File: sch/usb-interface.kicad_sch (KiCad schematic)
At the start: 4 parts, among them IC1 USB2244I-AEZG-06

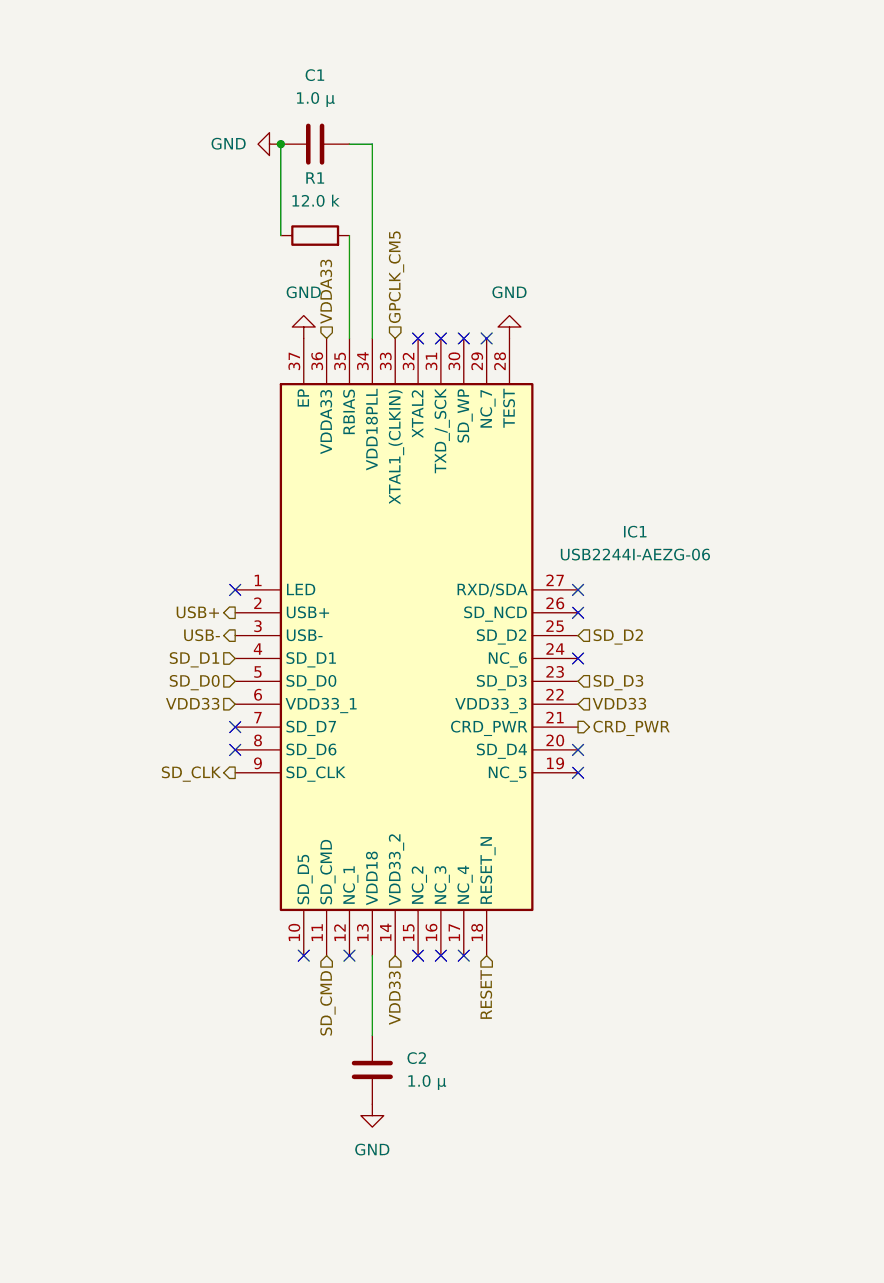
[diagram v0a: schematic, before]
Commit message: Added ports to CM5 and USB interface and connected them
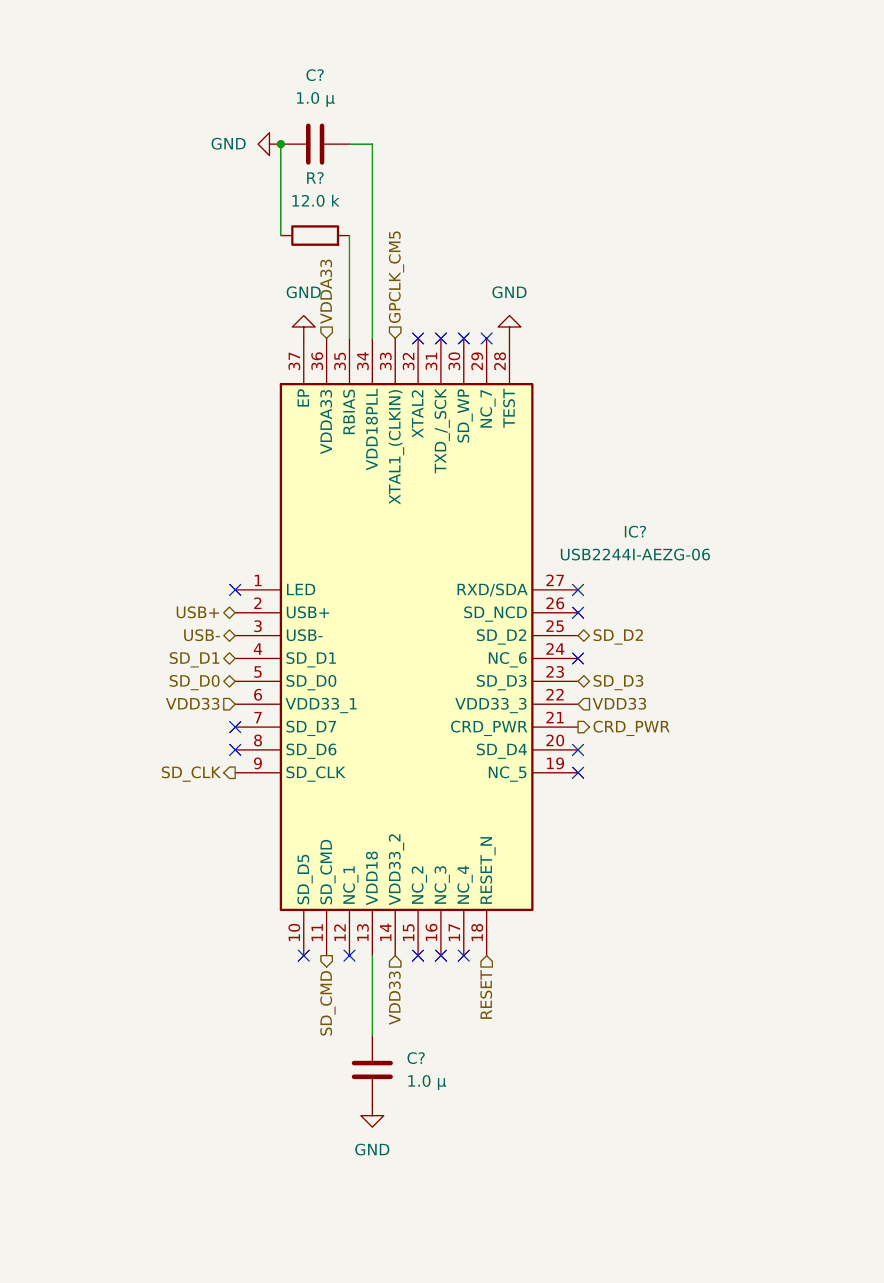
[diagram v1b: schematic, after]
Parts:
- renumbered C1 to C?, C2 to C?, IC1 to IC?, R1 to R?
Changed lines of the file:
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@@
 	)
 	(hierarchical_label "SD_D1"
-		(shape input)
+		(shape bidirectional)
 		(at 68.58 92.71 180)
 		(effects
@@
 	)
 	(hierarchical_label "SD_CMD"
-		(shape input)
+		(shape output)
 		(at 78.74 125.73 270)
 		(effects
@@
 	)
 	(hierarchical_label "SD_D3"
-		(shape input)
+		(shape bidirectional)
 		(at 106.68 95.25 0)
 		(effects
@@
 	)
 	(hierarchical_label "USB-"
-		(shape output)
+		(shape bidirectional)
 		(at 68.58 90.17 180)
 		(effects
@@
 	)
 	(hierarchical_label "SD_D0"
-		(shape input)
+		(shape bidirectional)
 		(at 68.58 95.25 180)
 		(effects
@@
 	)
 	(hierarchical_label "SD_D2"
-		(shape input)
+		(shape bidirectional)
 		(at 106.68 90.17 0)
 		(effects
@@
 	)
 	(hierarchical_label "USB+"
-		(shape output)
+		(shape bidirectional)
 		(at 68.58 87.63 180)
 		(effects
@@
 		(dnp no)
 		(fields_autoplaced yes)
-		(property "Reference" "#PWR04"
+		(property "Reference" "#PWR?"
 			(at 83.82 148.59 0)
 			(effects
@@
 		)
 		(instances
+			(project "audiograb"
+				(path "/c46c2311-6d4b-411d-b012-c7730eac136d/53f9c81a-1433-4854-9dfc-932cf29aee40"
+					(reference "#PWR?")
+					(unit 1)
+				)
+			)
 			(project "usb-interface"
 				(path "/eaea460a-c66f-4f33-a920-83ec112e8ee3"
@@
 		(dnp no)
 		(fields_autoplaced yes)
-		(property "Reference" "C1"
+		(property "Reference" "C?"
 			(at 77.47 27.94 90)
 			(effects
@@
 		)
 		(instances
+			(project "audiograb"
+				(path "/c46c2311-6d4b-411d-b012-c7730eac136d/53f9c81a-1433-4854-9dfc-932cf29aee40"
+					(reference "C?")
+					(unit 1)
+				)
+			)
 			(project ""
 				(path "/eaea460a-c66f-4f33-a920-83ec112e8ee3"
@@
 		(dnp no)
 		(fields_autoplaced yes)
-		(property "Reference" "C2"
+		(property "Reference" "C?"
 			(at 87.63 137.1599 0)
 			(effects
@@
 		)
 		(instances
+			(project "audiograb"
+				(path "/c46c2311-6d4b-411d-b012-c7730eac136d/53f9c81a-1433-4854-9dfc-932cf29aee40"
+					(reference "C?")
+					(unit 1)
+				)
+			)
 			(project ""
 				(path "/eaea460a-c66f-4f33-a920-83ec112e8ee3"
@@
 		(dnp no)
 		(fields_autoplaced yes)
-		(property "Reference" "R1"
+		(property "Reference" "R?"
 			(at 77.47 39.37 90)
 			(effects
@@
 		)
 		(instances
+			(project "audiograb"
+				(path "/c46c2311-6d4b-411d-b012-c7730eac136d/53f9c81a-1433-4854-9dfc-932cf29aee40"
+					(reference "R?")
+					(unit 1)
+				)
+			)
 			(project ""
 				(path "/eaea460a-c66f-4f33-a920-83ec112e8ee3"
@@
 		(dnp no)
 		(fields_autoplaced yes)
-		(property "Reference" "#PWR02"
+		(property "Reference" "#PWR?"
 			(at 99.06 50.8 0)
 			(effects
@@
 		)
 		(instances
+			(project "audiograb"
+				(path "/c46c2311-6d4b-411d-b012-c7730eac136d/53f9c81a-1433-4854-9dfc-932cf29aee40"
+					(reference "#PWR?")
+					(unit 1)
+				)
+			)
 			(project "usb-interface"
 				(path "/eaea460a-c66f-4f33-a920-83ec112e8ee3"
@@
 		(dnp no)
 		(fields_autoplaced yes)
-		(property "Reference" "#PWR01"
+		(property "Reference" "#PWR?"
 			(at 76.2 50.8 0)
 			(effects
@@
 		)
 		(instances
+			(project "audiograb"
+				(path "/c46c2311-6d4b-411d-b012-c7730eac136d/53f9c81a-1433-4854-9dfc-932cf29aee40"
+					(reference "#PWR?")
+					(unit 1)
+				)
+			)
 			(project ""
 				(path "/eaea460a-c66f-4f33-a920-83ec112e8ee3"
@@
 		(dnp no)
 		(fields_autoplaced yes)
-		(property "Reference" "#PWR03"
+		(property "Reference" "#PWR?"
 			(at 67.31 35.56 0)
 			(effects
@@
 		)
 		(instances
+			(project "audiograb"
+				(path "/c46c2311-6d4b-411d-b012-c7730eac136d/53f9c81a-1433-4854-9dfc-932cf29aee40"
+					(reference "#PWR?")
+					(unit 1)
+				)
+			)
 			(project "usb-interface"
 				(path "/eaea460a-c66f-4f33-a920-83ec112e8ee3"
@@
 		(dnp no)
 		(fields_autoplaced yes)
-		(property "Reference" "IC1"
+		(property "Reference" "IC?"
 			(at 113.03 78.6698 0)
 			(effects
@@
 		)
 		(instances
+			(project "audiograb"
+				(path "/c46c2311-6d4b-411d-b012-c7730eac136d/53f9c81a-1433-4854-9dfc-932cf29aee40"
+					(reference "IC?")
+					(unit 1)
+				)
+			)
 			(project ""
 				(path "/eaea460a-c66f-4f33-a920-83ec112e8ee3"

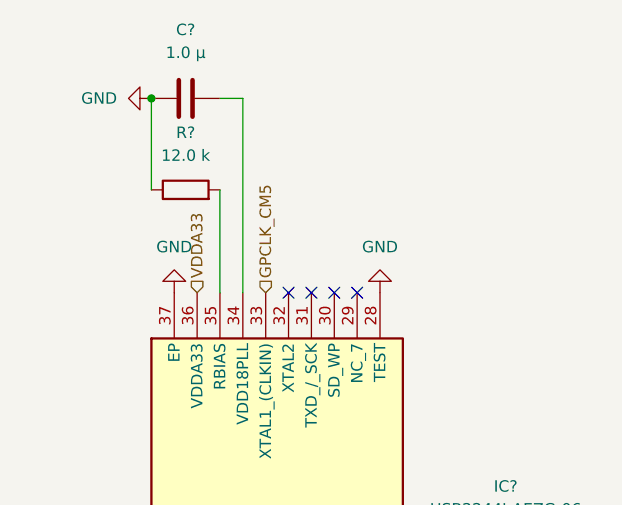
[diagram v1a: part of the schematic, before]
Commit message: Added more ports to the CM5 and connected them
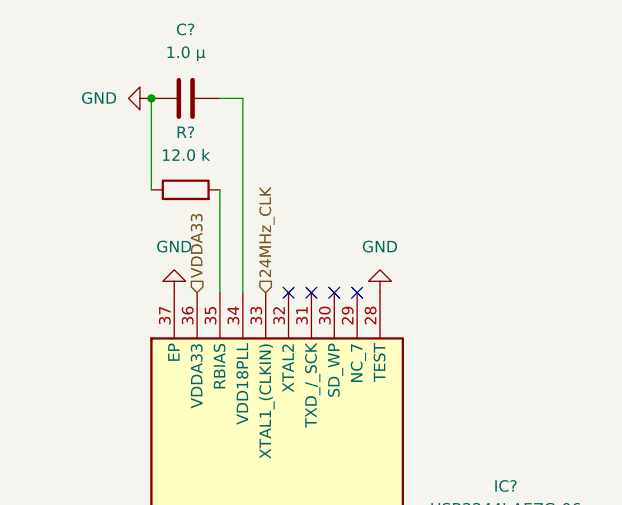
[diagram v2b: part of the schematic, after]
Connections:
- net GPCLK_CM5 renamed 24MHz_CLK
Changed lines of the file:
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@@
 		)
 	)
-	(hierarchical_label "GPCLK_CM5"
+	(hierarchical_label "24MHz_CLK"
 		(shape input)
 		(at 86.36 57.15 90)

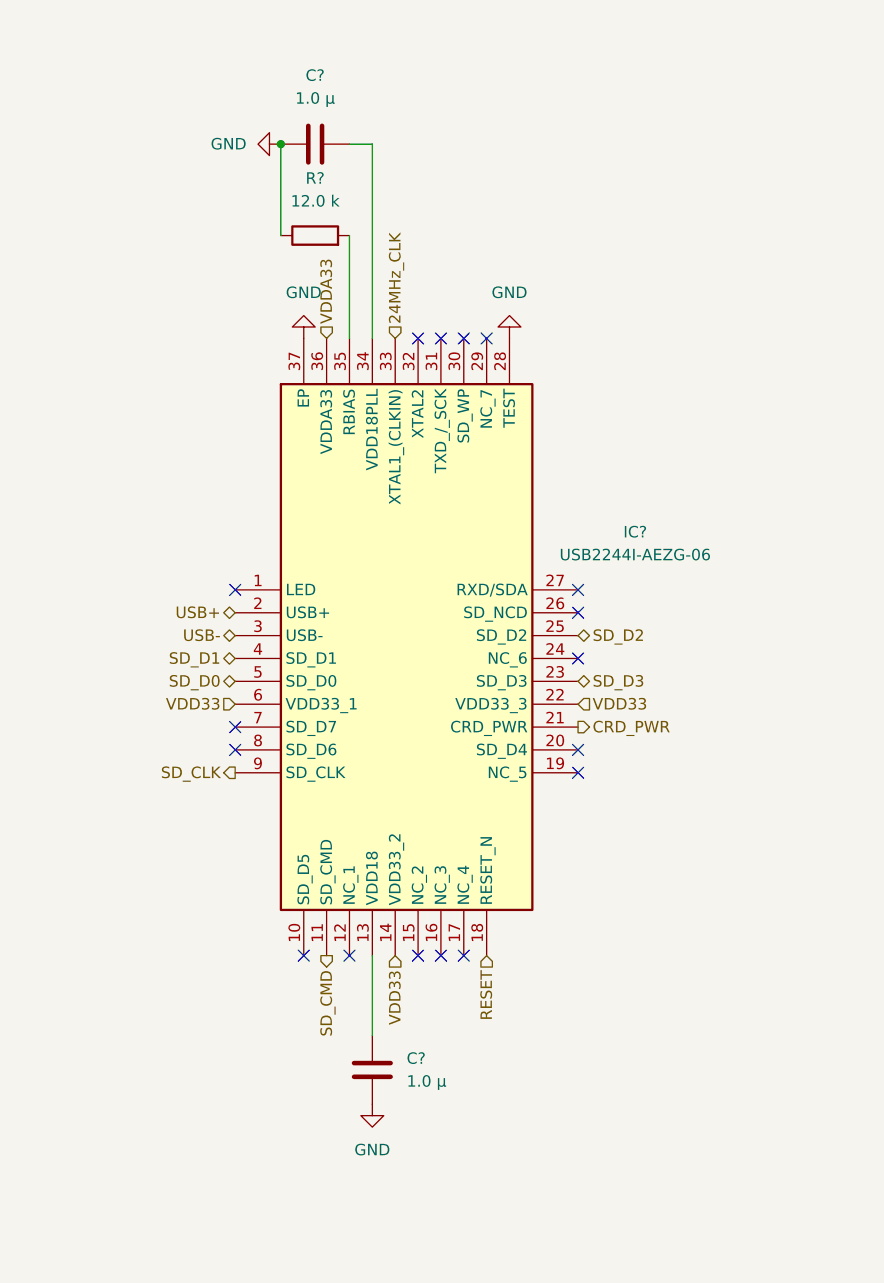
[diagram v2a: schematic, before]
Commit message: added cap footprints and part numbers
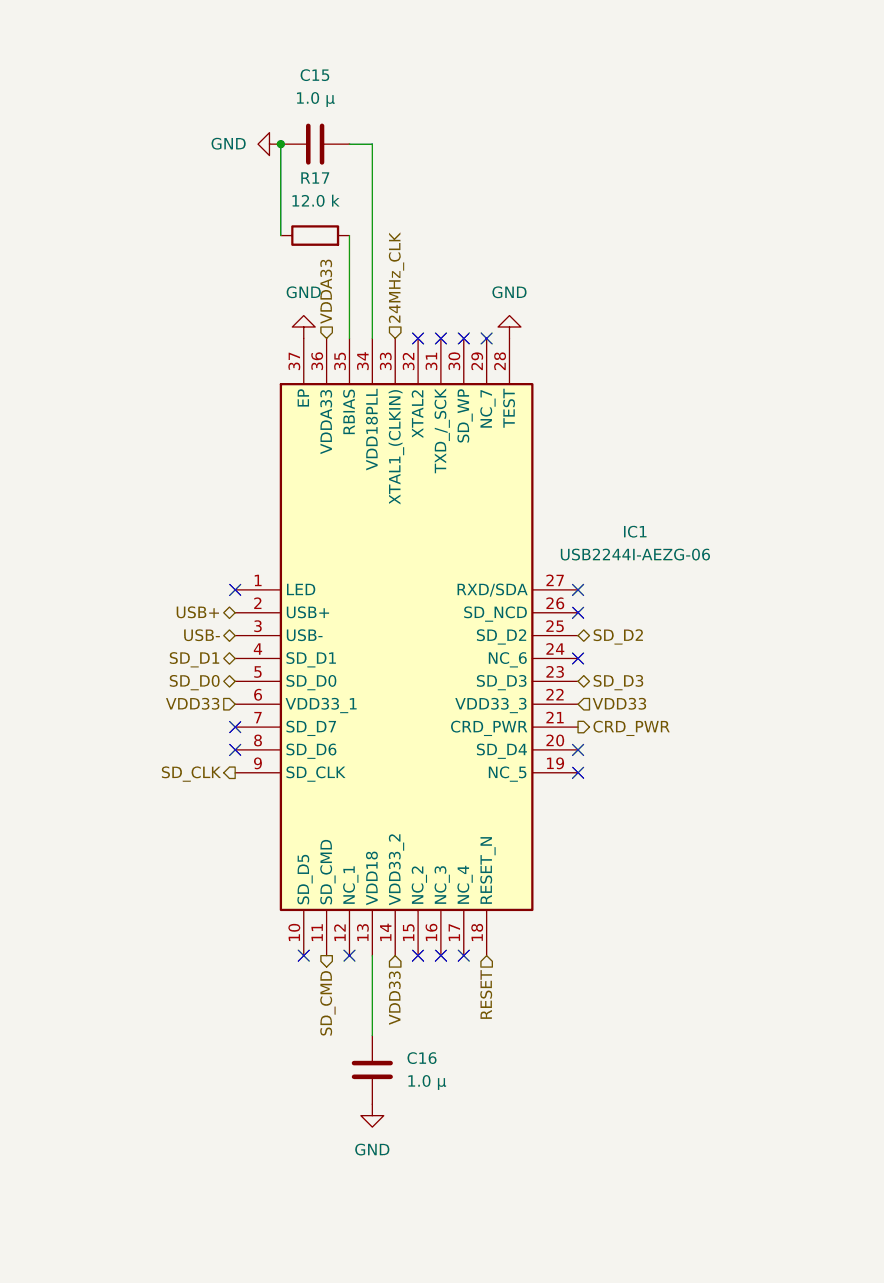
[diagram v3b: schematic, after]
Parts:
- C15, C16: renamed from C?; footprint (none) -> Capacitor_SMD:C_0603_1608Metric; MPN (none) -> CL10B105KP8NNNC
- gave numbers to parts that had none: 2
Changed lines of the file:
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@@
 		(dnp no)
 		(fields_autoplaced yes)
-		(property "Reference" "#PWR?"
+		(property "Reference" "#PWR060"
 			(at 83.82 148.59 0)
 			(effects
@@
 			(project "audiograb"
 				(path "/c46c2311-6d4b-411d-b012-c7730eac136d/53f9c81a-1433-4854-9dfc-932cf29aee40"
-					(reference "#PWR?")
+					(reference "#PWR060")
 					(unit 1)
 				)
@@
 		(dnp no)
 		(fields_autoplaced yes)
-		(property "Reference" "C?"
+		(property "Reference" "C15"
 			(at 77.47 27.94 90)
 			(effects
@@
 			)
 		)
-		(property "Footprint" ""
+		(property "Footprint" "Capacitor_SMD:C_0603_1608Metric"
 			(at 81.28 34.5948 0)
 			(effects
@@
 		(property "Description" "Unpolarized capacitor"
 			(at 77.47 35.56 0)
+			(effects
+				(font
+					(size 1.27 1.27)
+				)
+				(hide yes)
+			)
+		)
+		(property "MPN" "CL10B105KP8NNNC"
+			(at 77.47 35.56 90)
 			(effects
 				(font
@@
 			(project "audiograb"
 				(path "/c46c2311-6d4b-411d-b012-c7730eac136d/53f9c81a-1433-4854-9dfc-932cf29aee40"
-					(reference "C?")
+					(reference "C15")
 					(unit 1)
 				)
@@
 		(dnp no)
 		(fields_autoplaced yes)
-		(property "Reference" "C?"
+		(property "Reference" "C16"
 			(at 87.63 137.1599 0)
 			(effects
@@
 			)
 		)
-		(property "Footprint" ""
+		(property "Footprint" "Capacitor_SMD:C_0603_1608Metric"
 			(at 84.7852 142.24 0)
 			(effects
@@
 		)
 		(property "Description" "Unpolarized capacitor"
+			(at 83.82 138.43 0)
+			(effects
+				(font
+					(size 1.27 1.27)
+				)
+				(hide yes)
+			)
+		)
+		(property "MPN" "CL10B105KP8NNNC"
 			(at 83.82 138.43 0)
 			(effects
@@
 			(project "audiograb"
 				(path "/c46c2311-6d4b-411d-b012-c7730eac136d/53f9c81a-1433-4854-9dfc-932cf29aee40"
-					(reference "C?")
+					(reference "C16")
 					(unit 1)
 				)
@@
 		(dnp no)
 		(fields_autoplaced yes)
-		(property "Reference" "R?"
+		(property "Reference" "R17"
 			(at 77.47 39.37 90)
 			(effects
@@
 			(project "audiograb"
 				(path "/c46c2311-6d4b-411d-b012-c7730eac136d/53f9c81a-1433-4854-9dfc-932cf29aee40"
-					(reference "R?")
+					(reference "R17")
 					(unit 1)
 				)
@@
 		(dnp no)
 		(fields_autoplaced yes)
-		(property "Reference" "#PWR?"
+		(property "Reference" "#PWR061"
 			(at 99.06 50.8 0)
 			(effects
@@
 			(project "audiograb"
 				(path "/c46c2311-6d4b-411d-b012-c7730eac136d/53f9c81a-1433-4854-9dfc-932cf29aee40"
-					(reference "#PWR?")
+					(reference "#PWR061")
 					(unit 1)
 				)
@@
 		(dnp no)
 		(fields_autoplaced yes)
-		(property "Reference" "#PWR?"
+		(property "Reference" "#PWR059"
 			(at 76.2 50.8 0)
 			(effects
@@
 			(project "audiograb"
 				(path "/c46c2311-6d4b-411d-b012-c7730eac136d/53f9c81a-1433-4854-9dfc-932cf29aee40"
-					(reference "#PWR?")
+					(reference "#PWR059")
 					(unit 1)
 				)
@@
 		(dnp no)
 		(fields_autoplaced yes)
-		(property "Reference" "#PWR?"
+		(property "Reference" "#PWR058"
 			(at 67.31 35.56 0)
 			(effects
@@
 			(project "audiograb"
 				(path "/c46c2311-6d4b-411d-b012-c7730eac136d/53f9c81a-1433-4854-9dfc-932cf29aee40"
-					(reference "#PWR?")
+					(reference "#PWR058")
 					(unit 1)
 				)
@@
 		(dnp no)
 		(fields_autoplaced yes)
-		(property "Reference" "IC?"
+		(property "Reference" "IC1"
 			(at 113.03 78.6698 0)
 			(effects
@@
 			(project "audiograb"
 				(path "/c46c2311-6d4b-411d-b012-c7730eac136d/53f9c81a-1433-4854-9dfc-932cf29aee40"
-					(reference "IC?")
-					(unit 1)
-				)
+					(reference "IC1")
+					(unit 1)
+				)

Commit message: added footprints fore resistors
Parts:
- R17: footprint (none) -> Resistor_SMD:R_0603_1608Metric; MPN (none) -> RC0603FR-0712KL
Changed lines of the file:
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@@
 			)
 		)
-		(property "Footprint" ""
+		(property "Footprint" "Resistor_SMD:R_0603_1608Metric"
 			(at 77.47 47.498 90)
 			(effects
@@
 			(effects
 				(font
+					(size 1.27 1.27)
+				)
+				(hide yes)
+			)
+		)
+		(property "MPN" "RC0603FR-0712KL"
+			(at 77.47 45.72 90)
+			(effects
+				(font
